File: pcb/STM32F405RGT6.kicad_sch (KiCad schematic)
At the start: 18 parts, among them U1 STM32F405RGTx, Y1 8MHz

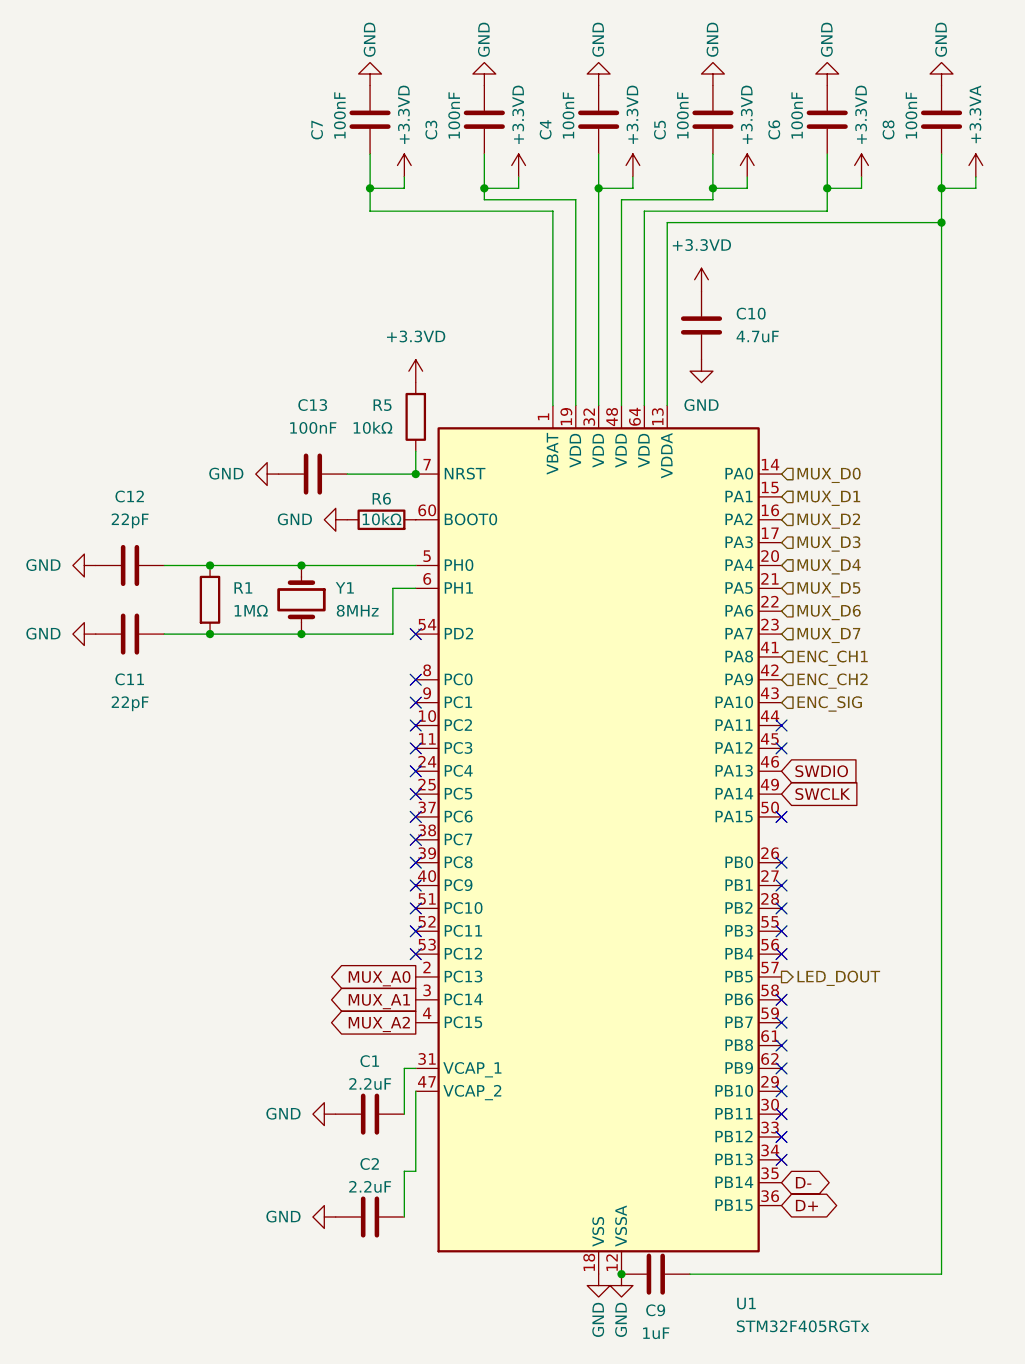
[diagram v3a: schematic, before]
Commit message: feat: assigned footprints for each symbol and switch
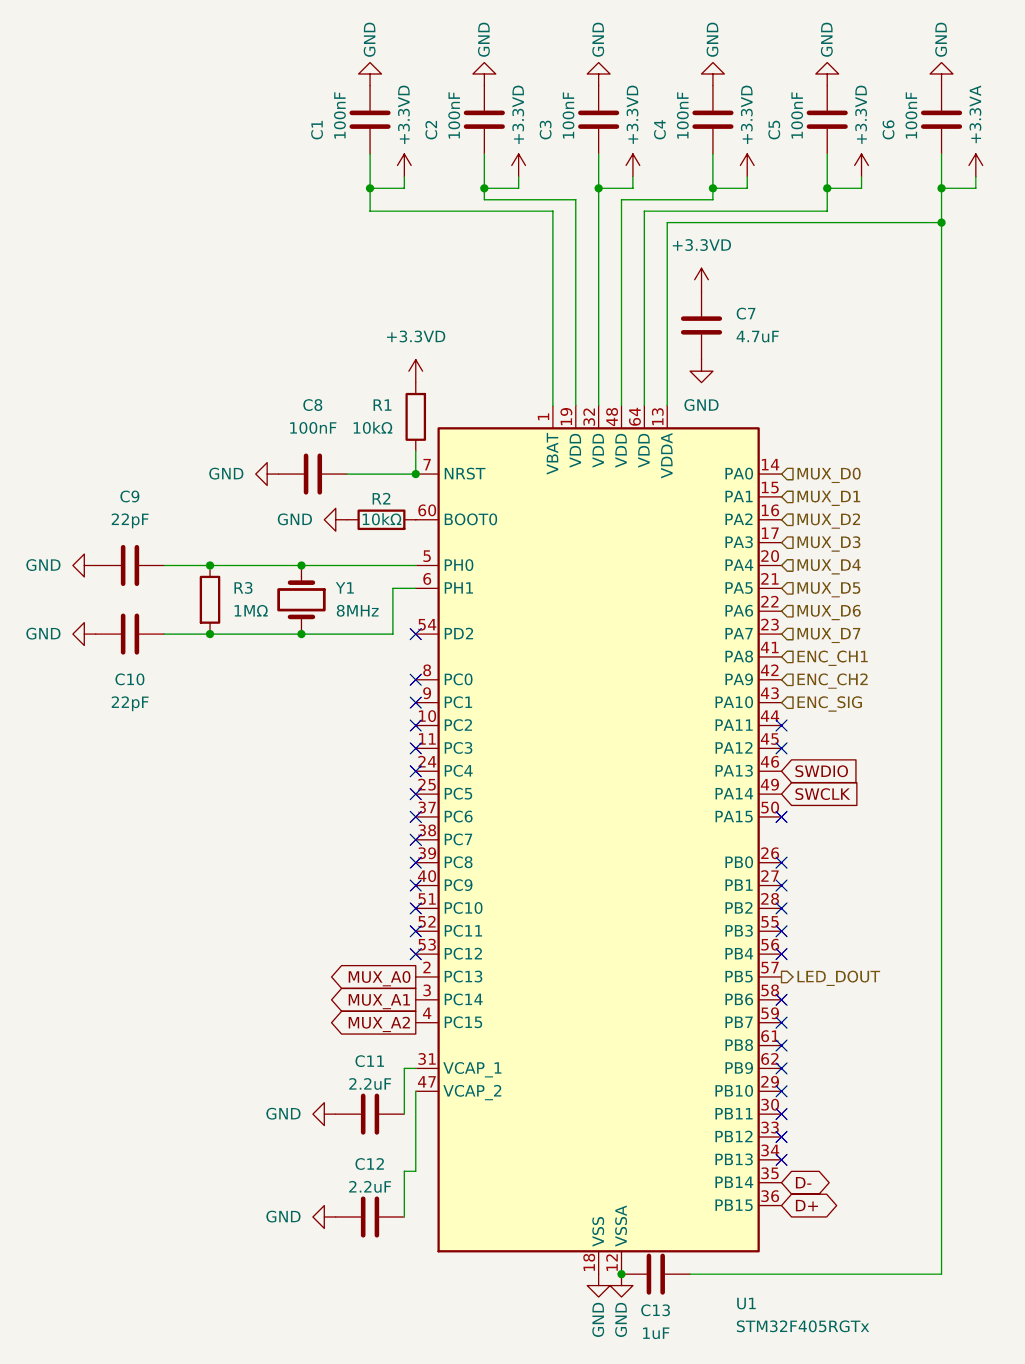
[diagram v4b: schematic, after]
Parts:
- C1: renamed from C7; footprint (none) -> Capacitor_SMD:C_0402_1005Metric
- C10: renamed from C11; footprint (none) -> Capacitor_SMD:C_0402_1005Metric
- C11: renamed from C1; footprint (none) -> Capacitor_SMD:C_0603_1608Metric
- C12: renamed from C2; footprint (none) -> Capacitor_SMD:C_0603_1608Metric
- C13: renamed from C9; footprint (none) -> Capacitor_SMD:C_0603_1608Metric
- C2: renamed from C3; footprint (none) -> Capacitor_SMD:C_0402_1005Metric
- C3: renamed from C4; footprint (none) -> Capacitor_SMD:C_0402_1005Metric
- C4: renamed from C5; footprint (none) -> Capacitor_SMD:C_0402_1005Metric
- C5: renamed from C6; footprint (none) -> Capacitor_SMD:C_0402_1005Metric
- C6: renamed from C8; footprint (none) -> Capacitor_SMD:C_0402_1005Metric
- C7: renamed from C10; footprint (none) -> Capacitor_SMD:C_0603_1608Metric
- C8: renamed from C13; footprint (none) -> Capacitor_SMD:C_0402_1005Metric
- C9: renamed from C12; footprint (none) -> Capacitor_SMD:C_0402_1005Metric
- R1: renamed from R5; footprint (none) -> Resistor_SMD:R_0603_1608Metric
- R2: renamed from R6; footprint (none) -> Resistor_SMD:R_0603_1608Metric
- R3: renamed from R1; footprint (none) -> Resistor_SMD:R_0603_1608Metric
- Y1: footprint (none) -> Crystal:Crystal_SMD_3225-4Pin_3.2x2.5mm
